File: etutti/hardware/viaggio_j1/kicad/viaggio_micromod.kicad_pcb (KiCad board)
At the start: 4 copper layers, 246.5 x 95 mm, 177 parts, among them J101 91302-42-067RCE, J201 TYPE-C-31-M-12, J202 S3B-PH-SM4-TB, J301 PJ-327A 5JJ, J501 alto-falante (fios), Q201 AO3401A, Q202 AO3400A, Q203 AO3401A, SW1 Gateron_Magnetic_MX_1u, SW10 Gateron_Magnetic_MX_1u, SW11 Gateron_Magnetic_MX_1u, SW12 Gateron_Magnetic_MX_1u, SW13 Gateron_Magnetic_MX_1u, SW14 Gateron_Magnetic_MX_1u, SW15 Gateron_Magnetic_MX_1u, SW16 Gateron_Magnetic_MX_1u, SW17 Gateron_Magnetic_MX_1u, SW18 Gateron_Magnetic_MX_1u, SW19 Gateron_Magnetic_MX_1u, SW2 Gateron_Magnetic_MX_1u, SW20 Gateron_Magnetic_MX_1u, SW21 Gateron_Magnetic_MX_1u, SW22 Gateron_Magnetic_MX_1u, SW23 Gateron_Magnetic_MX_1u, SW24 Gateron_Magnetic_MX_1u, SW25 Gateron_Magnetic_MX_1u, SW26 Gateron_Magnetic_MX_1u, SW27 Gateron_Magnetic_MX_1u, SW28 Gateron_Magnetic_MX_1u, SW3 Gateron_Magnetic_MX_1u, SW4 Gateron_Magnetic_MX_1u, SW401 EC11E18244A5, SW402 EC11E18244A5, SW403 Program, SW5 Gateron_Magnetic_MX_1u, SW6 Gateron_Magnetic_MX_1u, SW7 Gateron_Magnetic_MX_1u, SW8 Gateron_Magnetic_MX_1u, SW9 Gateron_Magnetic_MX_1u, U201 USBLC6-2SC6, U202 BQ24074RGTR, U203 74LVC1G08, U204 TPS63001DRCR, U301 SGTL5000XNLA3, U302 XC6206P182MR, U501 MAX98357AETE+T, U601 74HC4067PW, U602 74HC4067PW, U603 74LVC1G04, U604 74LVC1G08, U605 74LVC1G08, U701 TMAG5253BA3IQDMRR, U702 TMAG5253BA3IQDMRR, U703 TMAG5253BA3IQDMRR, U704 TMAG5253BA3IQDMRR, U705 TMAG5253BA3IQDMRR, U706 TMAG5253BA3IQDMRR, U707 TMAG5253BA3IQDMRR, U708 TMAG5253BA3IQDMRR, U709 TMAG5253BA3IQDMRR, U710 TMAG5253BA3IQDMRR, U711 TMAG5253BA3IQDMRR, U712 TMAG5253BA3IQDMRR, U713 TMAG5253BA3IQDMRR, U714 TMAG5253BA3IQDMRR, U715 TMAG5253BA3IQDMRR, U716 TMAG5253BA3IQDMRR, U717 TMAG5253BA3IQDMRR, U718 TMAG5253BA3IQDMRR, U719 TMAG5253BA3IQDMRR, U720 TMAG5253BA3IQDMRR, U721 TMAG5253BA3IQDMRR, U722 TMAG5253BA3IQDMRR, U723 TMAG5253BA3IQDMRR, U724 TMAG5253BA3IQDMRR, U725 TMAG5253BA3IQDMRR, U726 TMAG5253BA3IQDMRR, U727 TMAG5253BA3IQDMRR, U728 TMAG5253BA3IQDMRR

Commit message: eTutti Viaggio J1: GND and +3V3 copper on J's routed board
cobre.py (KiCad python, no router or path search) adds to
viaggio_j1/kicad/viaggio_micromod.kicad_pcb only:
- GND pours on F.Cu and B.Cu, a +3V3 pour on In2 (In1 GND untouched,
  only refilled), clearance 0.25;
- 941 GND stitching vias 0.5/0.3 (5 mm grid + one per island);
- 46 vias with straight stubs for GND/+3V3 pins left unconnected;
- removes the 6 dangling vias the DRC reported.
J's 1314 tracks, 207 remaining vias and all footprints are unchanged.

DRC: no new clearance/short errors; unconnected 237 -> 51 (GND 9,
+3V3 18, other nets untouched). J's 13 track_width items remain, plus
one dangling OUT_K03 stub that ended on a removed via. Report: COBRE.md.

Co-Authored-By: Claude Opus 5.5 <noreply@anthropic.com>
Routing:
- net +3V3: track 204.0 -> 245.1 mm, vias 4 -> 47
- net GND: track 0.00 -> 5.45 mm, vias 0 -> 944
- net PROG: vias 3 -> 2
- net OUT_K03: vias 1 -> 0
- net MUX_S2: vias 4 -> 3
- net HP_R: vias 3 -> 2
- net HP_L: vias 2 -> 1
- net EN_A: vias 15 -> 14
- added copper zone on In2.Cu, net +3V3
- added copper zone on B.Cu, net GND
- added copper zone on F.Cu, net GND

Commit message: eTutti Viaggio J1 rota restante: lote 1 — VSYS, VBAT e GND do carregador
rota_restante.py (KiCad 10 python): 3-layer grid A* (F.Cu, In2.Cu, B.Cu),
exact pcbnew clearance check, splice save. Lot 1 closes 5 GND islands,
VSYS to the amplifier (76 mm, 0.8) and 2 VBAT links. BB_L1/BB_L2 and the
VSYS to U204.5 are walled by J's +3V3 track at x 71.7 on B.Cu.
DRC: 13 track_width (J's), 1 track_dangling (OUT_K03 stub), unrouted 51 -> 43.

Co-Authored-By: Claude Opus 5.5 <noreply@anthropic.com>
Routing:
- net VSYS: track 26.3 -> 103.8 mm, vias 2 -> 5
- net VBAT: track 0.50 -> 28.0 mm, vias 0 -> 5
- net GND: track 5.45 -> 8.05 mm, vias 944 -> 945

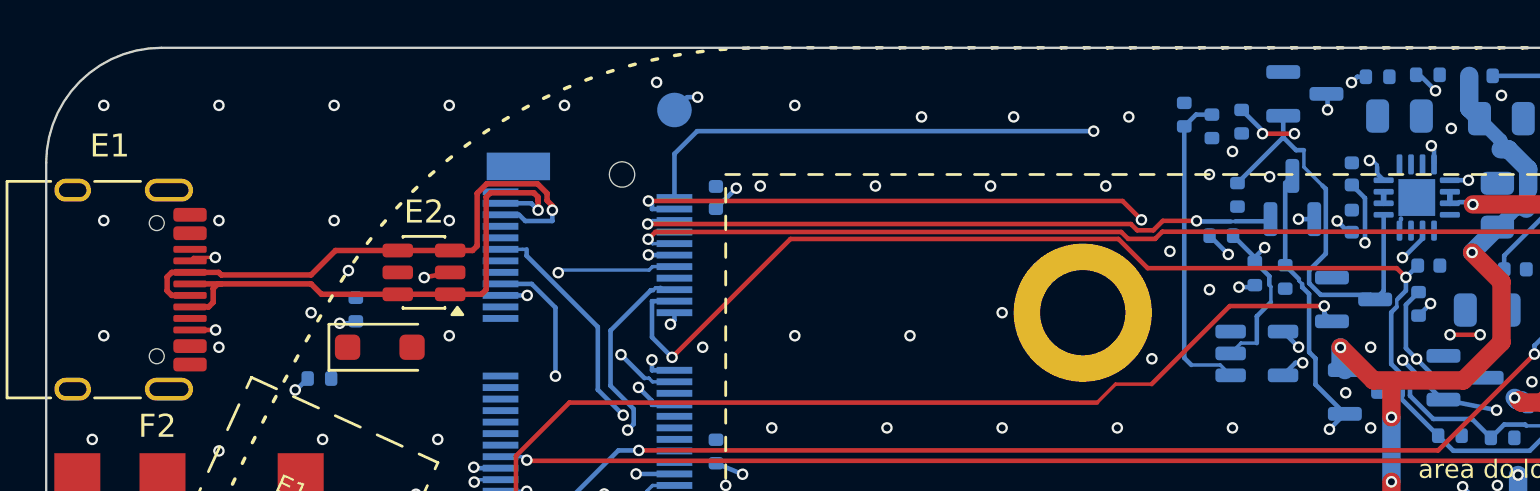
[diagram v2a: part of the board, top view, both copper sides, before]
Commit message: eTutti Viaggio J1 rota restante: lote 2 — VBUS
VBUS 10 -> 1 (J201 to J101, U201, D201 and the charger input, 0.8 mm,
5 necks of 0.5 mm at pin entries outside the .kicad_dru courtyards).
One GND island cut by the new tracks joined in the same lot. R206.1 left
out (walled). DRC: no new clearance/short/hole; unrouted 43 -> 34.

Co-Authored-By: Claude Opus 5.5 <noreply@anthropic.com>
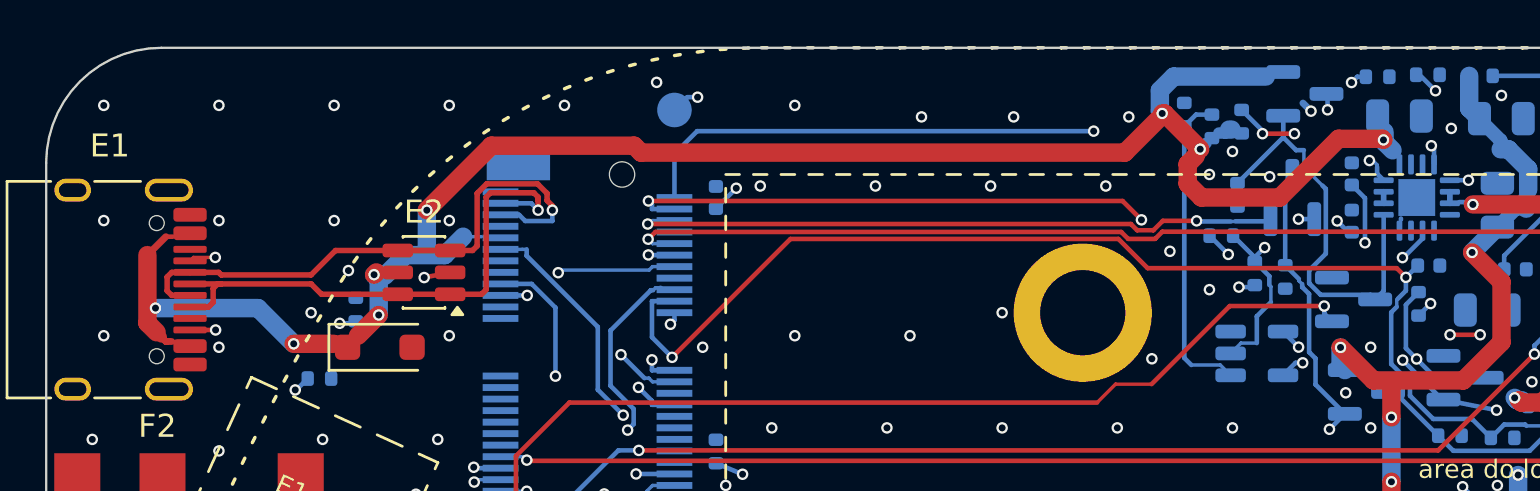
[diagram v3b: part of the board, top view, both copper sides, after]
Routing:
- net VBUS: track 0.00 -> 79.3 mm, vias 0 -> 8
- net GND: track 8.05 -> 8.55 mm, vias 945 -> 946
